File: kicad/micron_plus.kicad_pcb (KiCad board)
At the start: 2 copper layers, 163.8 x 123.2 mm, 90 parts, among them J1 Conn_02x17_Odd_Even, J2 Cliff DC10A, Q1 2N2905A, Q2 2N2905A, Q3 2N3904, Q4 2N3904, U1 MC68A21, U10 74LS00, U11 7406, U12 HM6264LP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

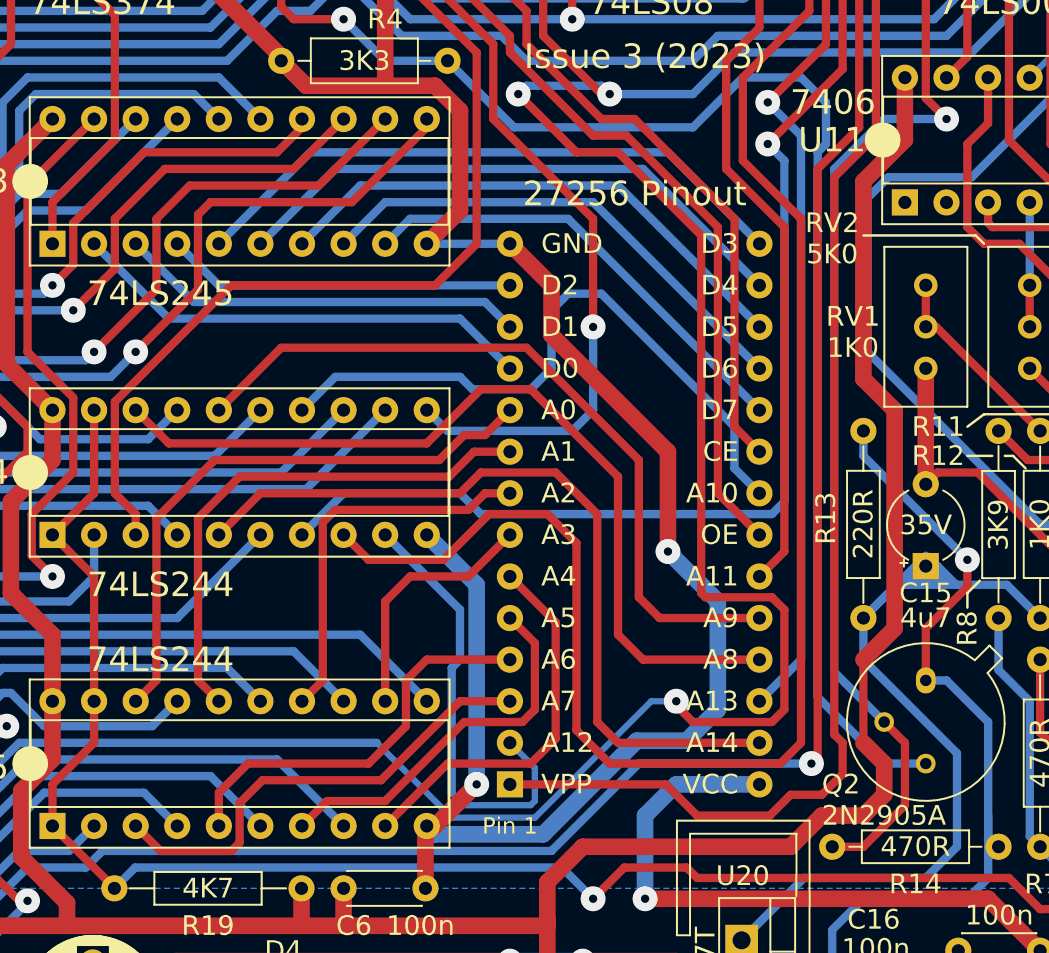
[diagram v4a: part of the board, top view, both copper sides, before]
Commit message: KiCAD: Use 0.95mm holes for ZIF socket
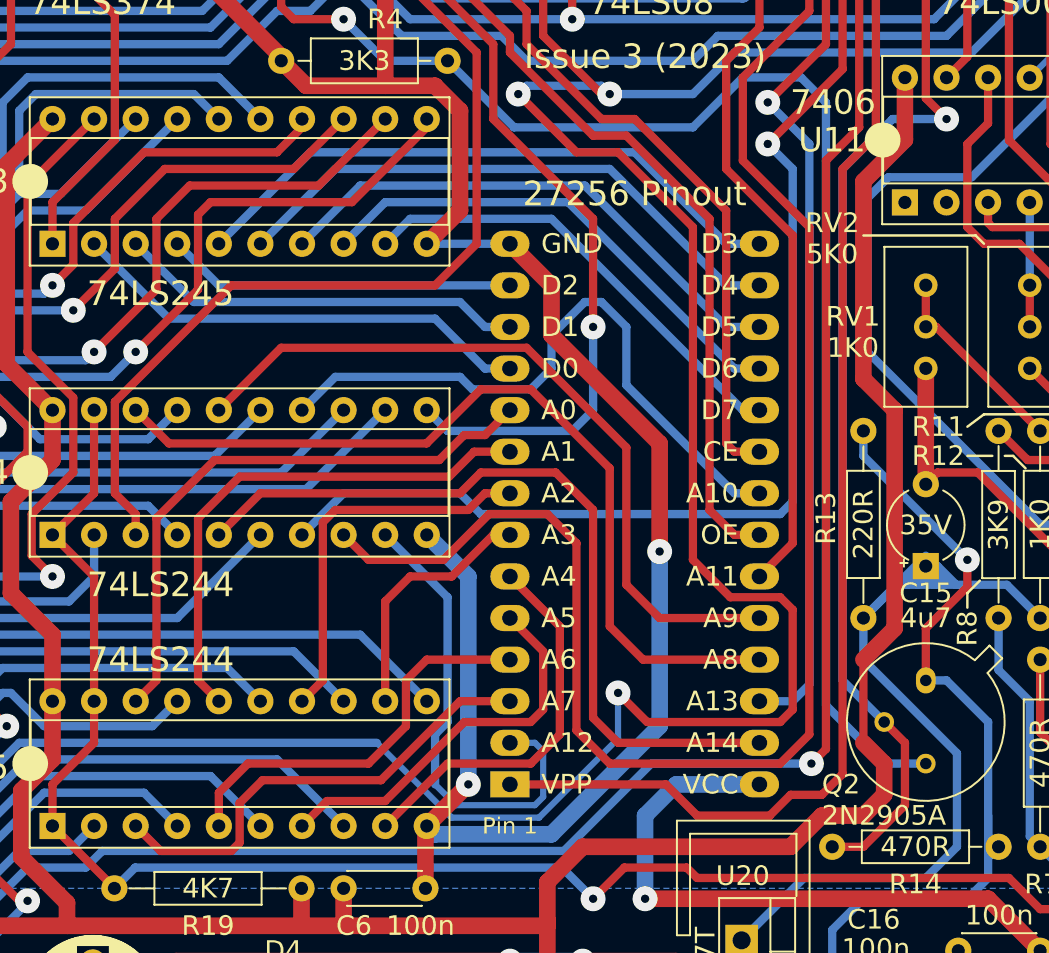
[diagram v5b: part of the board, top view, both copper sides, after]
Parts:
- U17: footprint Package_DIP:DIP-28_W15.24mm_Socket -> custom_footprints:DIP-28_W15.24mm_Socket_LongPads
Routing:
- net GND: track 683.1 -> 678.0 mm
- net /1MHz Bus and PIA Interface/Addr12: track 287.3 -> 289.6 mm
- net /Main Logic and Eprom Socket/Eprom2: track 27.5 -> 29.5 mm
- net /Main Logic and Eprom Socket/Eprom26VCC: track 162.4 -> 164.0 mm
- net /Control Latches/Eprom20: track 55.5 -> 56.4 mm
- net /Main Logic and Eprom Socket/Eprom22VPP: track 75.5 -> 76.4 mm
- net /Main Logic and Eprom Socket/Eprom26: track 185.7 -> 186.4 mm
- net /Main Logic and Eprom Socket/Eprom21: track 40.1 -> 39.4 mm
- net Net-(Q2-Pad2): track 85.2 -> 84.5 mm
- net /Main Logic and Eprom Socket/Eprom5: track 23.4 -> 24.1 mm

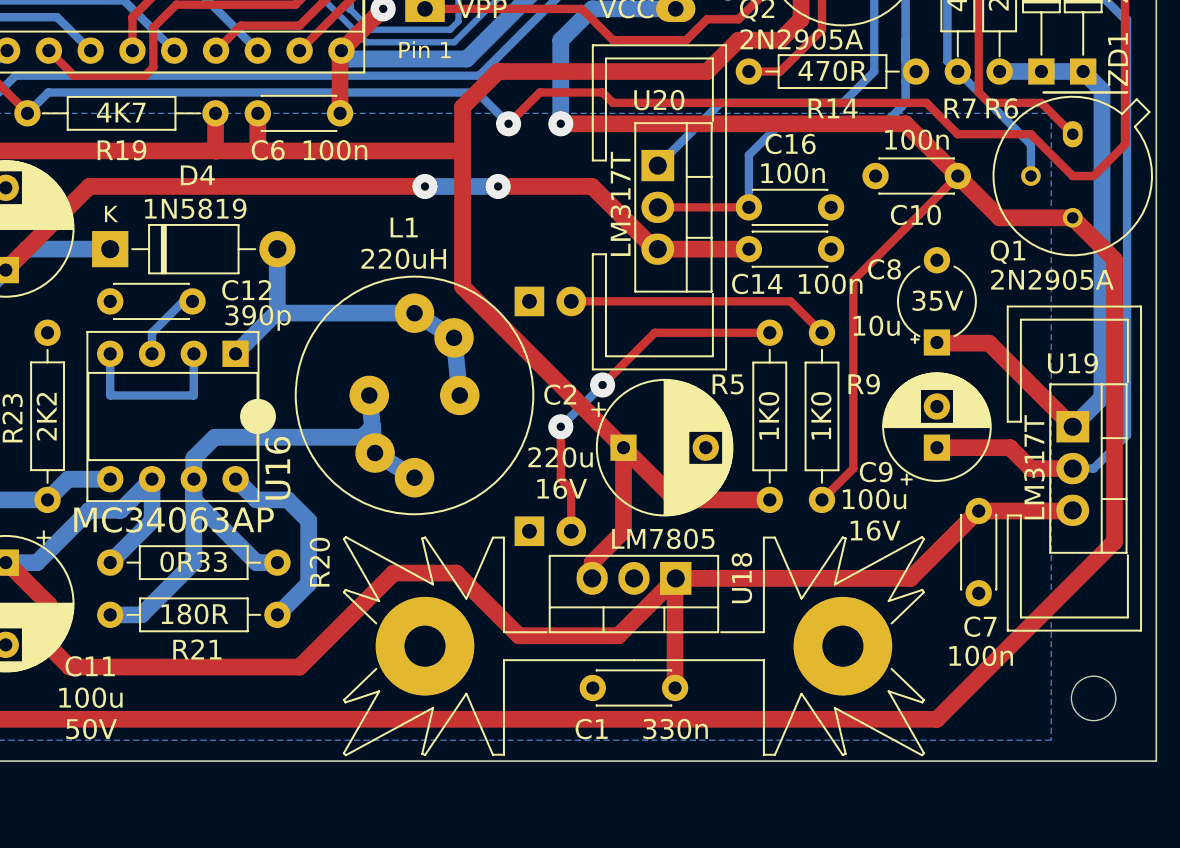
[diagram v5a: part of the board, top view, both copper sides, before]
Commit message: KiCAD: silk screen
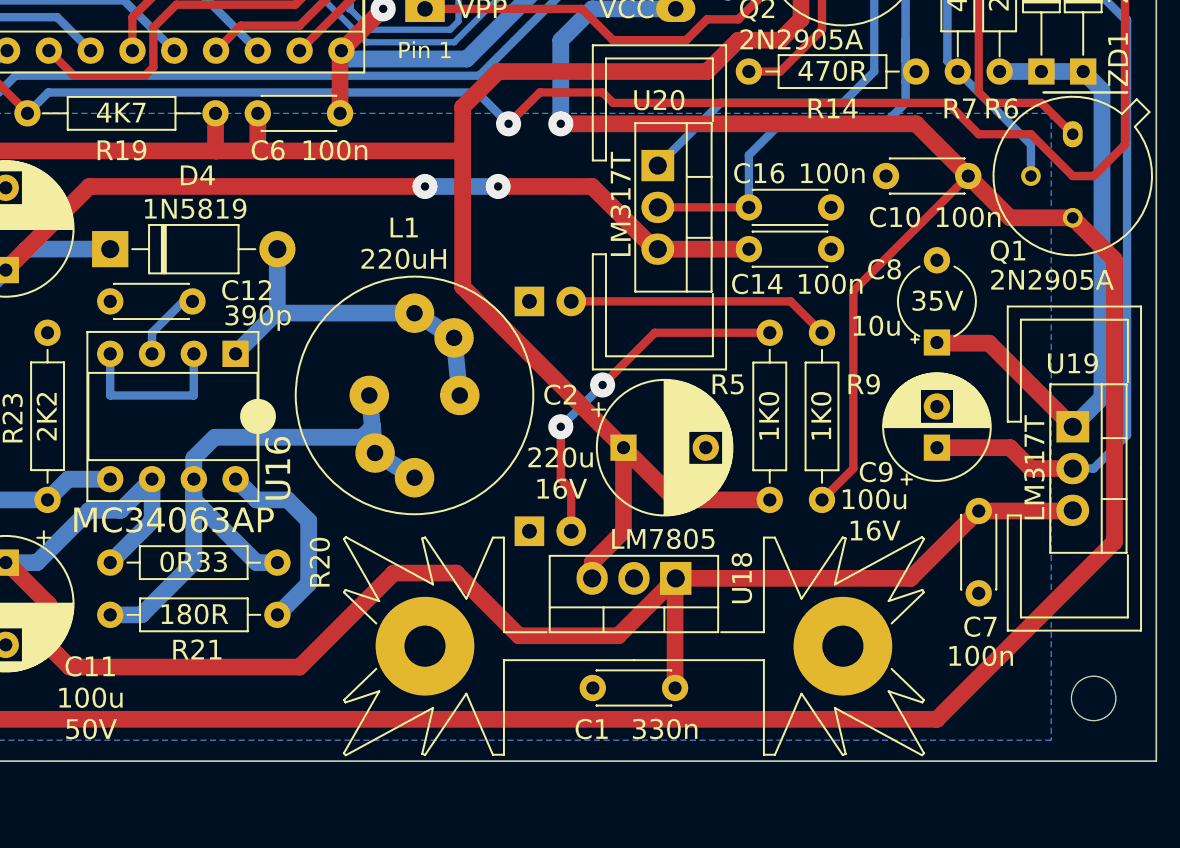
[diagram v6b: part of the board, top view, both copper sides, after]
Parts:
- moved C10 0.63 mm to (193.0, 109.2)
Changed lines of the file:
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@@
     (property "Sheetname" "Power Supply")
     (attr through_hole)
-    (fp_text reference "C16" (at 2.54 -3.81) (layer "F.SilkS")
+    (fp_text reference "C16" (at 0.635 -2.032) (layer "F.SilkS")
       (effects (font (size 1.2 1.2) (thickness 0.15)))
     )
-    (fp_text value "100n" (at 2.667 -2.032) (layer "F.SilkS")
+    (fp_text value "100n" (at 5.08 -2.032) (layer "F.SilkS")
       (effects (font (size 1.2 1.2) (thickness 0.15)))
     )
@@
       (effects (font (size 1.2 1.2) (thickness 0.15)))
     )
-    (fp_text user "K" (at 0 -2.1) (layer "F.SilkS")
+    (fp_text user "K" (at 0 -2.1) (layer "F.SilkS") hide
       (effects (font (size 1 1) (thickness 0.15)))
     )
@@
   )
   (footprint "Capacitor_THT:C_Disc_D4.3mm_W1.9mm_P5.00mm" (layer "F.Cu")
-    (at 192.405 109.22 180)
+    (at 193.04 109.22 180)
     (descr "C, Disc series, Radial, pin pitch=5.00mm, , diameter*width=4.3*1.9mm^2, Capacitor, http://www.vishay.com/docs/45233/krseries.pdf")
     (tags "C Disc series Radial pin pitch 5.00mm  diameter 4.3mm width 1.9mm Capacitor")
@@
     (property "Sheetname" "Power Supply")
     (attr through_hole)
-    (fp_text reference "C10" (at 2.54 -2.413) (layer "F.SilkS")
+    (fp_text reference "C10" (at 4.445 -2.54) (layer "F.SilkS")
       (effects (font (size 1.2 1.2) (thickness 0.15)))
     )
-    (fp_text value "100n" (at 2.5 2.159) (layer "F.SilkS")
+    (fp_text value "100n" (at 0 -2.54) (layer "F.SilkS")
       (effects (font (size 1.2 1.2) (thickness 0.15)))
     )
@@
       (effects (font (size 1.2 1.2) (thickness 0.15)))
     )
-    (fp_text value "330n" (at -0.04 -2.54) (layer "F.SilkS")
+    (fp_text value "330n" (at 0.595 -2.54) (layer "F.SilkS")
       (effects (font (size 1.2 1.2) (thickness 0.15)))
     )
@@
   (segment (start 201.168 104.013) (end 201.168 122.682) (width 1.016) (layer "B.Cu") (net 4))
   (segment (start 194.945 102.87) (end 197.485 102.87) (width 1.016) (layer "B.Cu") (net 4))
-  (segment (start 194.945 111.76) (end 192.405 109.22) (width 1.016) (layer "F.Cu") (net 5))
+  (segment (start 193.04 109.22) (end 189.865 106.045) (width 1.016) (layer "F.Cu") (net 5))
+  (segment (start 189.865 106.045) (end 168.275 106.045) (width 1.016) (layer "F.Cu") (net 5))
   (segment (start 51.435 142.24) (end 191.135 142.24) (width 1.016) (layer "F.Cu") (net 5))
   (segment (start 42.164 132.969) (end 51.435 142.24) (width 1.016) (layer "F.Cu") (net 5))
   (segment (start 96.774 24.13) (end 54.61 24.13) (width 1.016) (layer "F.Cu") (net 5))
-  (segment (start 189.23 106.045) (end 192.405 109.22) (width 1.016) (layer "F.Cu") (net 5))
-  (segment (start 184.15 128.905) (end 186.055 127) (width 0.508) (layer "F.Cu") (net 5))
-  (segment (start 186.055 127) (end 186.055 115.57) (width 0.508) (layer "F.Cu") (net 5))
   (segment (start 191.135 142.24) (end 201.93 131.445) (width 1.016) (layer "F.Cu") (net 5))
-  (segment (start 168.275 106.045) (end 189.23 106.045) (width 1.016) (layer "F.Cu") (net 5))
-  (segment (start 199.39 111.76) (end 194.945 111.76) (width 1.016) (layer "F.Cu") (net 5))
+  (segment (start 186.055 116.205) (end 186.055 127) (width 0.508) (layer "F.Cu") (net 5))
+  (segment (start 193.04 109.22) (end 186.055 116.205) (width 0.508) (layer "F.Cu") (net 5))
   (segment (start 101.6 28.956) (end 96.774 24.13) (width 1.016) (layer "F.Cu") (net 5))
-  (segment (start 186.055 115.57) (end 192.405 109.22) (width 0.508) (layer "F.Cu") (net 5))
+  (segment (start 186.055 127) (end 184.15 128.905) (width 0.508) (layer "F.Cu") (net 5))
   (segment (start 201.93 131.445) (end 201.93 114.3) (width 1.016) (layer "F.Cu") (net 5))
+  (segment (start 199.39 111.76) (end 195.58 111.76) (width 1.016) (layer "F.Cu") (net 5))
   (segment (start 42.164 36.576) (end 42.164 132.969) (width 1.016) (layer "F.Cu") (net 5))
+  (segment (start 195.58 111.76) (end 193.04 109.22) (width 1.016) (layer "F.Cu") (net 5))
   (segment (start 54.61 24.13) (end 42.164 36.576) (width 1.016) (layer "F.Cu") (net 5))
   (segment (start 201.93 114.3) (end 199.39 111.76) (width 1.016) (layer "F.Cu") (net 5))
@@
   (segment (start 131.572 30.48) (end 133.35 32.258) (width 0.508) (layer "B.Cu") (net 46))
   (segment (start 63.5 130.81) (end 55.88 125.095) (width 0.508) (layer "B.Cu") (net 46))
+  (segment (start 165.1 106.045) (end 167.005 104.14) (width 0.508) (layer "F.Cu") (net 47))
   (segment (start 102.87 37.846) (end 102.87 41.783) (width 0.508) (layer "F.Cu") (net 47))
-  (segment (start 196.85 106.68) (end 199.39 109.22) (width 0.508) (layer "F.Cu") (net 47))
+  (segment (start 170.815 104.14) (end 171.45 104.775) (width 0.508) (layer "F.Cu") (net 47))
+  (segment (start 200.66 109.22) (end 202.565 107.315) (width 0.508) (layer "F.Cu") (net 47))
   (segment (start 134.62 76.2) (end 134.62 81.28) (width 0.508) (layer "F.Cu") (net 47))
-  (segment (start 202.565 107.315) (end 202.565 80.01) (width 0.508) (layer "F.Cu") (net 47))
   (segment (start 102.108 37.084) (end 102.87 37.846) (width 0.508) (layer "F.Cu") (net 47))
-  (segment (start 199.39 109.22) (end 200.66 109.22) (width 0.508) (layer "F.Cu") (net 47))
   (segment (start 198.12 59.944) (end 196.845 58.669) (width 0.508) (layer "F.Cu") (net 47))
   (segment (start 198.12 64.516) (end 198.12 59.944) (width 0.508) (layer "F.Cu") (net 47))
   (segment (start 198.628 65.024) (end 198.12 64.516) (width 0.508) (layer "F.Cu") (net 47))
-  (segment (start 171.45 104.775) (end 190.5 104.775) (width 0.508) (layer "F.Cu") (net 47))
-  (segment (start 170.815 104.14) (end 171.45 104.775) (width 0.508) (layer "F.Cu") (net 47))
-  (segment (start 165.1 106.045) (end 167.005 104.14) (width 0.508) (layer "F.Cu") (net 47))
   (segment (start 196.845 58.669) (end 196.845 55.895) (width 0.508) (layer "F.Cu") (net 47))
+  (segment (start 202.565 107.315) (end 202.565 80.01) (width 0.508) (layer "F.Cu") (net 47))
   (segment (start 109.982 23.114) (end 102.108 30.988) (width 0.508) (layer "F.Cu") (net 47))
   (segment (start 132.08 101.6) (end 135.86 105.38) (width 0.508) (layer "F.Cu") (net 47))
-  (segment (start 190.5 104.775) (end 192.405 106.68) (width 0.508) (layer "F.Cu") (net 47))
-  (segment (start 167.005 104.14) (end 170.815 104.14) (width 0.508) (layer "F.Cu") (net 47))
-  (segment (start 192.405 106.68) (end 196.85 106.68) (width 0.508) (layer "F.Cu") (net 47))
+  (segment (start 201.803 79.248) (end 201.168 79.248) (width 0.508) (layer "F.Cu") (net 47))
+  (segment (start 196.85 106.68) (end 199.39 109.22) (width 0.508) (layer "F.Cu") (net 47))
   (segment (start 202.057 79.248) (end 203.2 78.105) (width 0.508) (layer "F.Cu") (net 47))
+  (segment (start 167.005 104.14) (end 170.815 104.14) (width 0.508) (layer "F.Cu") (net 47))
   (segment (start 202.184 65.024) (end 203.454 63.754) (width 0.508) (layer "F.Cu") (net 47))
   (segment (start 101.6 43.053) (end 101.6 48.26) (width 0.508) (layer "F.Cu") (net 47))
@@
   (segment (start 191.643 79.248) (end 201.168 79.248) (width 0.508) (layer "F.Cu") (net 47))
   (segment (start 194.31 23.114) (end 203.454 32.258) (width 0.508) (layer "F.Cu") (net 47))
+  (segment (start 193.675 106.68) (end 196.85 106.68) (width 0.508) (layer "F.Cu") (net 47))
   (segment (start 109.982 23.114) (end 194.31 23.114) (width 0.381) (layer "F.Cu") (net 47))
   (segment (start 102.87 41.783) (end 101.6 43.053) (width 0.508) (layer "F.Cu") (net 47))
@@
   (segment (start 189.865 77.47) (end 191.643 79.248) (width 0.508) (layer "F.Cu") (net 47))
   (segment (start 134.62 81.28) (end 132.08 83.82) (width 0.508) (layer "F.Cu") (net 47))
-  (segment (start 201.803 79.248) (end 201.168 79.248) (width 0.508) (layer "F.Cu") (net 47))
   (segment (start 132.08 101.6) (end 132.08 99.06) (width 0.508) (layer "F.Cu") (net 47))
-  (segment (start 202.565 80.01) (end 201.803 79.248) (width 0.508) (layer "F.Cu") (net 47))
   (segment (start 201.168 79.248) (end 202.057 79.248) (width 0.508) (layer "F.Cu") (net 47))
+  (segment (start 191.77 104.775) (end 193.675 106.68) (width 0.508) (layer "F.Cu") (net 47))
   (segment (start 203.2 66.04) (end 202.184 65.024) (width 0.508) (layer "F.Cu") (net 47))
   (segment (start 202.184 65.024) (end 198.628 65.024) (width 0.508) (layer "F.Cu") (net 47))
-  (segment (start 200.66 109.22) (end 202.565 107.315) (width 0.508) (layer "F.Cu") (net 47))
+  (segment (start 202.565 80.01) (end 201.803 79.248) (width 0.508) (layer "F.Cu") (net 47))
+  (segment (start 199.39 109.22) (end 200.66 109.22) (width 0.508) (layer "F.Cu") (net 47))
+  (segment (start 171.45 104.775) (end 191.77 104.775) (width 0.508) (layer "F.Cu") (net 47))
   (segment (start 203.454 32.258) (end 203.454 63.754) (width 0.508) (layer "F.Cu") (net 47))
   (segment (start 102.108 30.988) (end 102.108 37.084) (width 0.508) (layer "F.Cu") (net 47))
